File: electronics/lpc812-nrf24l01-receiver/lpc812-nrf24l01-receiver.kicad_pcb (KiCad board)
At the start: 2 copper layers, 25 x 29 mm, 21 parts, among them K1 BAT, K2 CH3, K3 TH, K4 ST, P1 NRF24L01+, SW1 ISP/BIND, U1 MCP1703, U2 LPC812, X1 16MHz

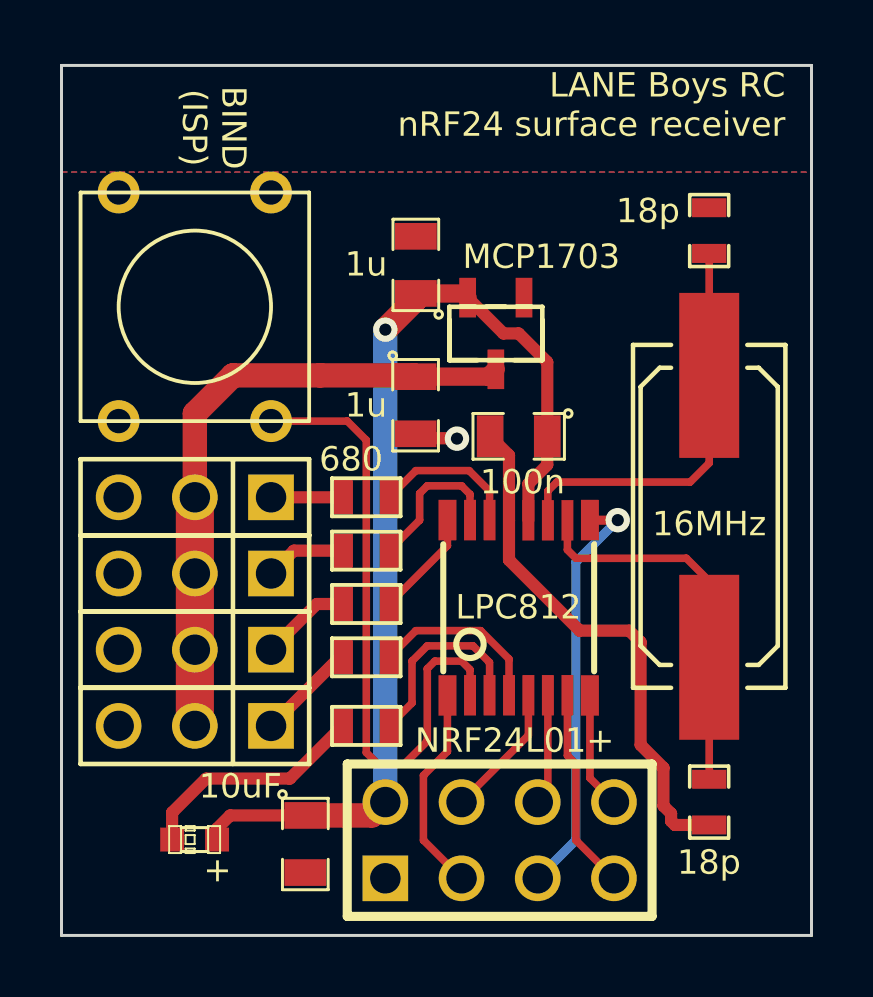
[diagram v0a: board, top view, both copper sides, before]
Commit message: More silk screen tweaking
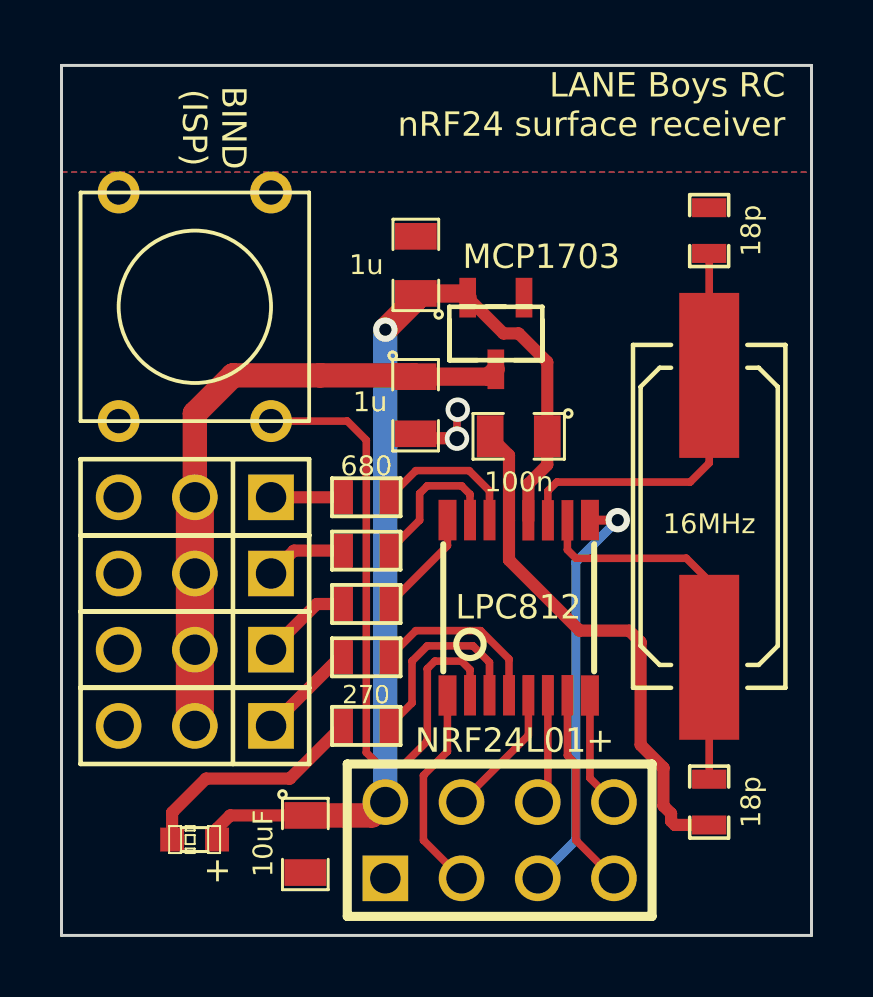
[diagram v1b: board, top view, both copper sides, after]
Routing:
- net VSS: track 19.0 -> 20.9 mm, vias 1 -> 2
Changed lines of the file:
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@@
     (thickness 1.6)
     (drawings 16)
-    (tracks 121)
+    (tracks 126)
     (zones 0)
     (modules 21)
@@
     (20 B.SilkS user hide)
     (21 F.SilkS user)
-    (22 B.Mask user)
-    (23 F.Mask user)
+    (22 B.Mask user hide)
+    (23 F.Mask user hide)
     (28 Edge.Cuts user)
   )
@@
       (effects (font (size 0.508 0.4572) (thickness 0.1143)))
     )
-    (fp_text value 18p (at 2.011 0.008 360) (layer F.SilkS)
-      (effects (font (size 0.8128 0.8128) (thickness 0.1778)))
+    (fp_text value 18p (at 0 -1.397 270) (layer F.SilkS)
+      (effects (font (size 0.6604 0.6604) (thickness 0.1524)))
     )
     (fp_line (start 0.50038 0.65024) (end 1.19888 0.65024) (layer F.SilkS) (width 0.11938))
@@
       (effects (font (size 0.8128 0.8128) (thickness 0.000001)))
     )
-    (fp_text value 18p (at 0.656 -2.04 180) (layer F.SilkS)
-      (effects (font (size 0.8128 0.8128) (thickness 0.1778)))
+    (fp_text value 18p (at 0 1.397 90) (layer F.SilkS)
+      (effects (font (size 0.6604 0.6604) (thickness 0.1524)))
     )
     (fp_line (start 0.50038 0.65024) (end 1.19888 0.65024) (layer F.SilkS) (width 0.11938))
@@
       (effects (font (size 0.50038 0.50038) (thickness 0.10922)))
     )
-    (fp_text value 10uF (at -1.926 2.167 360) (layer F.SilkS)
-      (effects (font (size 0.8128 0.8128) (thickness 0.1778)))
+    (fp_text value 10uF (at -0.021 1.405 270) (layer F.SilkS)
+      (effects (font (size 0.6604 0.6604) (thickness 0.1524)))
     )
     (fp_circle (center -1.651 0.762) (end -1.651 0.635) (layer F.SilkS) (width 0.09906))
@@
       (effects (font (size 0.508 0.4572) (thickness 0.1143)))
     )
-    (fp_text value 680 (at 0.508 1.27 180) (layer F.SilkS)
-      (effects (font (size 0.8128 0.8128) (thickness 0.1778)))
+    (fp_text value 680 (at 0 1.0414 180) (layer F.SilkS)
+      (effects (font (size 0.6604 0.6604) (thickness 0.1524)))
     )
     (fp_line (start -1.143 -0.635) (end 1.143 -0.635) (layer F.SilkS) (width 0.127))
@@
       (effects (font (size 0.8128 0.8128) (thickness 0.10922)))
     )
-    (fp_text value 1u (at 0.021 -1.659 180) (layer F.SilkS)
-      (effects (font (size 0.8128 0.8128) (thickness 0.1778)))
+    (fp_text value 1u (at 0 -1.651 180) (layer F.SilkS)
+      (effects (font (size 0.6604 0.6604) (thickness 0.1524)))
     )
     (fp_circle (center -1.651 0.762) (end -1.651 0.635) (layer F.SilkS) (width 0.09906))
@@
       (effects (font (size 0.50038 0.50038) (thickness 0.10922)))
     )
-    (fp_text value 100n (at -0.127 -1.524 180) (layer F.SilkS)
-      (effects (font (size 0.8128 0.8128) (thickness 0.1778)))
+    (fp_text value 100n (at 0 -1.524 180) (layer F.SilkS)
+      (effects (font (size 0.6604 0.6604) (thickness 0.1524)))
     )
     (fp_circle (center -1.651 0.762) (end -1.651 0.635) (layer F.SilkS) (width 0.09906))
@@
       (effects (font (size 0.50038 0.50038) (thickness 0.10922)))
     )
-    (fp_text value 1u (at 0 1.651 360) (layer F.SilkS)
-      (effects (font (size 0.8128 0.8128) (thickness 0.1778)))
+    (fp_text value 1u (at -0.106 1.516 360) (layer F.SilkS)
+      (effects (font (size 0.6604 0.6604) (thickness 0.1524)))
     )
     (fp_circle (center -1.651 0.762) (end -1.651 0.635) (layer F.SilkS) (width 0.09906))
@@
       (effects (font (size 0.508 0.4572) (thickness 0.1143)))
     )
-    (fp_text value 270 (at -1.778 1.905) (layer F.SilkS) hide
-      (effects (font (size 0.8128 0.8128) (thickness 0.1778)))
+    (fp_text value 270 (at -0.008 -1.037) (layer F.SilkS)
+      (effects (font (size 0.6096 0.6096) (thickness 0.1524)))
     )
     (fp_line (start -1.143 -0.635) (end 1.143 -0.635) (layer F.SilkS) (width 0.127))
@@
     )
     (fp_text value 16MHz (at -0.254 0 180) (layer F.SilkS)
-      (effects (font (size 0.8128 0.8128) (thickness 0.1778)))
+      (effects (font (size 0.6604 0.6604) (thickness 0.1524)))
     )
     (fp_line (start -4.953 -1.651) (end -4.953 -1.27) (layer F.SilkS) (width 0.15))
@@
   (segment (start 72.398 73.173) (end 70.747 73.173) (width 0.4064) (layer F.Cu) (net 21) (status 30))
   (segment (start 70.747 73.173) (end 69.985 73.935) (width 0.4064) (layer F.Cu) (net 21) (status 30))
+  (segment (start 76.1826 69.4392) (end 76.1826 68.4994) (width 0.254) (layer B.Cu) (net 22))
+  (segment (start 76.1699 69.4265) (end 76.1826 69.4392) (width 0.4064) (layer F.Cu) (net 22))
+  (via (at 76.1826 69.4392) (size 0.8128) (drill 0.5) (layers F.Cu B.Cu) (net 22))
   (segment (start 74.811 69.4265) (end 76.1699 69.4265) (width 0.4064) (layer F.Cu) (net 22) (status 10))
-  (via (at 76.1826 69.4392) (size 0.813) (layers F.Cu B.Cu) (net 22))
-  (segment (start 76.1699 69.4265) (end 76.1826 69.4392) (width 0.4064) (layer F.Cu) (net 22))
+  (segment (start 76.1826 68.4994) (end 76.1826 69.4392) (width 0.254) (layer F.Cu) (net 22))
+  (segment (start 76.208 68.474) (end 76.1826 68.4994) (width 0.254) (layer F.Cu) (net 22))
+  (via (at 76.208 68.474) (size 0.8128) (drill 0.5) (layers F.Cu B.Cu) (net 22))
+  (segment (start 76.1826 68.4994) (end 76.208 68.474) (width 0.254) (layer B.Cu) (net 22))
   (segment (start 77.91742 72.16208) (end 77.91742 69.99292) (width 0.4064) (layer F.Cu) (net 22) (status 10))
   (segment (start 77.91742 69.99292) (end 77.2875 69.363) (width 0.4064) (layer F.Cu) (net 22) (status 20))

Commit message: Fix via alignmnet, add LED to silk screen
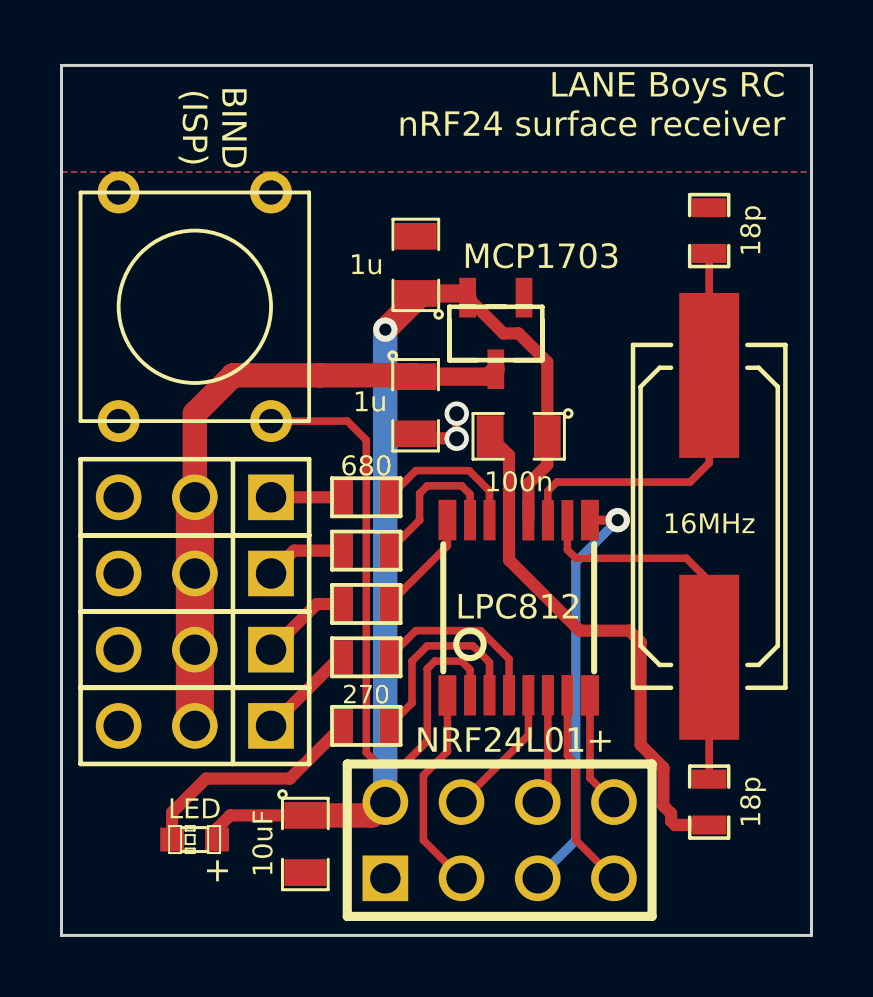
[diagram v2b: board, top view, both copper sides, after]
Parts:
- D1: value LED blue -> LED
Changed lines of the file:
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@@
       (effects (font (size 0.508 0.508) (thickness 0.127)))
     )
-    (fp_text value "LED blue" (at 0 1.016 180) (layer F.SilkS) hide
-      (effects (font (size 0.8128 0.8128) (thickness 0.1778)))
+    (fp_text value LED (at 0 1.016 180) (layer F.SilkS)
+      (effects (font (size 0.6604 0.6604) (thickness 0.1524)))
     )
     (fp_line (start 0.44958 -0.44958) (end 0.44958 0.44958) (layer F.SilkS) (width 0.06604))
@@
   (segment (start 72.398 73.173) (end 70.747 73.173) (width 0.4064) (layer F.Cu) (net 21) (status 30))
   (segment (start 70.747 73.173) (end 69.985 73.935) (width 0.4064) (layer F.Cu) (net 21) (status 30))
-  (segment (start 76.1826 69.4392) (end 76.1826 68.4994) (width 0.254) (layer B.Cu) (net 22))
-  (segment (start 76.1699 69.4265) (end 76.1826 69.4392) (width 0.4064) (layer F.Cu) (net 22))
-  (via (at 76.1826 69.4392) (size 0.8128) (drill 0.5) (layers F.Cu B.Cu) (net 22))
-  (segment (start 74.811 69.4265) (end 76.1699 69.4265) (width 0.4064) (layer F.Cu) (net 22) (status 10))
-  (segment (start 76.1826 68.4994) (end 76.1826 69.4392) (width 0.254) (layer F.Cu) (net 22))
-  (segment (start 76.208 68.474) (end 76.1826 68.4994) (width 0.254) (layer F.Cu) (net 22))
-  (via (at 76.208 68.474) (size 0.8128) (drill 0.5) (layers F.Cu B.Cu) (net 22))
-  (segment (start 76.1826 68.4994) (end 76.208 68.474) (width 0.254) (layer B.Cu) (net 22))
+  (segment (start 76.1746 69.4436) (end 76.1492 68.6308) (width 0.254) (layer B.Cu) (net 22))
+  (segment (start 76.1619 69.4309) (end 76.1746 69.4436) (width 0.4064) (layer F.Cu) (net 22))
+  (via (at 76.1746 69.4436) (size 0.8128) (drill 0.5) (layers F.Cu B.Cu) (net 22))
+  (segment (start 74.811 69.4265) (end 76.1619 69.4309) (width 0.4064) (layer F.Cu) (net 22) (status 10))
+  (segment (start 76.1492 68.6308) (end 76.1746 69.4436) (width 0.254) (layer F.Cu) (net 22))
+  (segment (start 76.1746 68.6054) (end 76.1492 68.6308) (width 0.254) (layer F.Cu) (net 22))
+  (via (at 76.1746 68.6054) (size 0.8128) (drill 0.5) (layers F.Cu B.Cu) (net 22))
+  (segment (start 76.1492 68.6308) (end 76.1746 68.6054) (width 0.254) (layer B.Cu) (net 22))
   (segment (start 77.91742 72.16208) (end 77.91742 69.99292) (width 0.4064) (layer F.Cu) (net 22) (status 10))
   (segment (start 77.91742 69.99292) (end 77.2875 69.363) (width 0.4064) (layer F.Cu) (net 22) (status 20))
